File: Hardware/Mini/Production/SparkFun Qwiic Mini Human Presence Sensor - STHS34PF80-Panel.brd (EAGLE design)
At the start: 175 x 132.6 mm, 2112 parts, among them J1 Qwiic, J10 Qwiic, J100 Qwiic, J101 Qwiic, J103 Qwiic, J104 Qwiic, J106 Qwiic, J107 Qwiic, J109 Qwiic, J11 Qwiic, J110 Qwiic, J112 Qwiic, J113 Qwiic, J115 Qwiic, J116 Qwiic, J118 Qwiic, J119 Qwiic, J121 Qwiic, J122 Qwiic, J124 Qwiic, J125 Qwiic, J127 Qwiic, J128 Qwiic, J13 Qwiic, J130 Qwiic, J131 Qwiic, J133 Qwiic, J134 Qwiic, J136 Qwiic, J137 Qwiic, J139 Qwiic, J14 Qwiic, J140 Qwiic, J142 Qwiic, J143 Qwiic, J145 Qwiic, J146 Qwiic, J148 Qwiic, J149 Qwiic, J151 Qwiic, J152 Qwiic, J154 Qwiic, J155 Qwiic, J157 Qwiic, J158 Qwiic, J16 Qwiic, J160 Qwiic, J161 Qwiic, J17 Qwiic, J19 Qwiic, J2 Qwiic, J20 Qwiic, J22 Qwiic, J23 Qwiic, J25 Qwiic, J26 Qwiic, J28 Qwiic, J29 Qwiic, J31 Qwiic, J32 Qwiic, J34 Qwiic, J35 Qwiic, J37 Qwiic, J38 Qwiic, J4 Qwiic, J40 Qwiic, J41 Qwiic, J43 Qwiic, J44 Qwiic, J46 Qwiic, J47 Qwiic, J49 Qwiic, J5 Qwiic, J50 Qwiic, J52 Qwiic, J53 Qwiic, J55 Qwiic, J56 Qwiic, J58 Qwiic, J59 Qwiic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

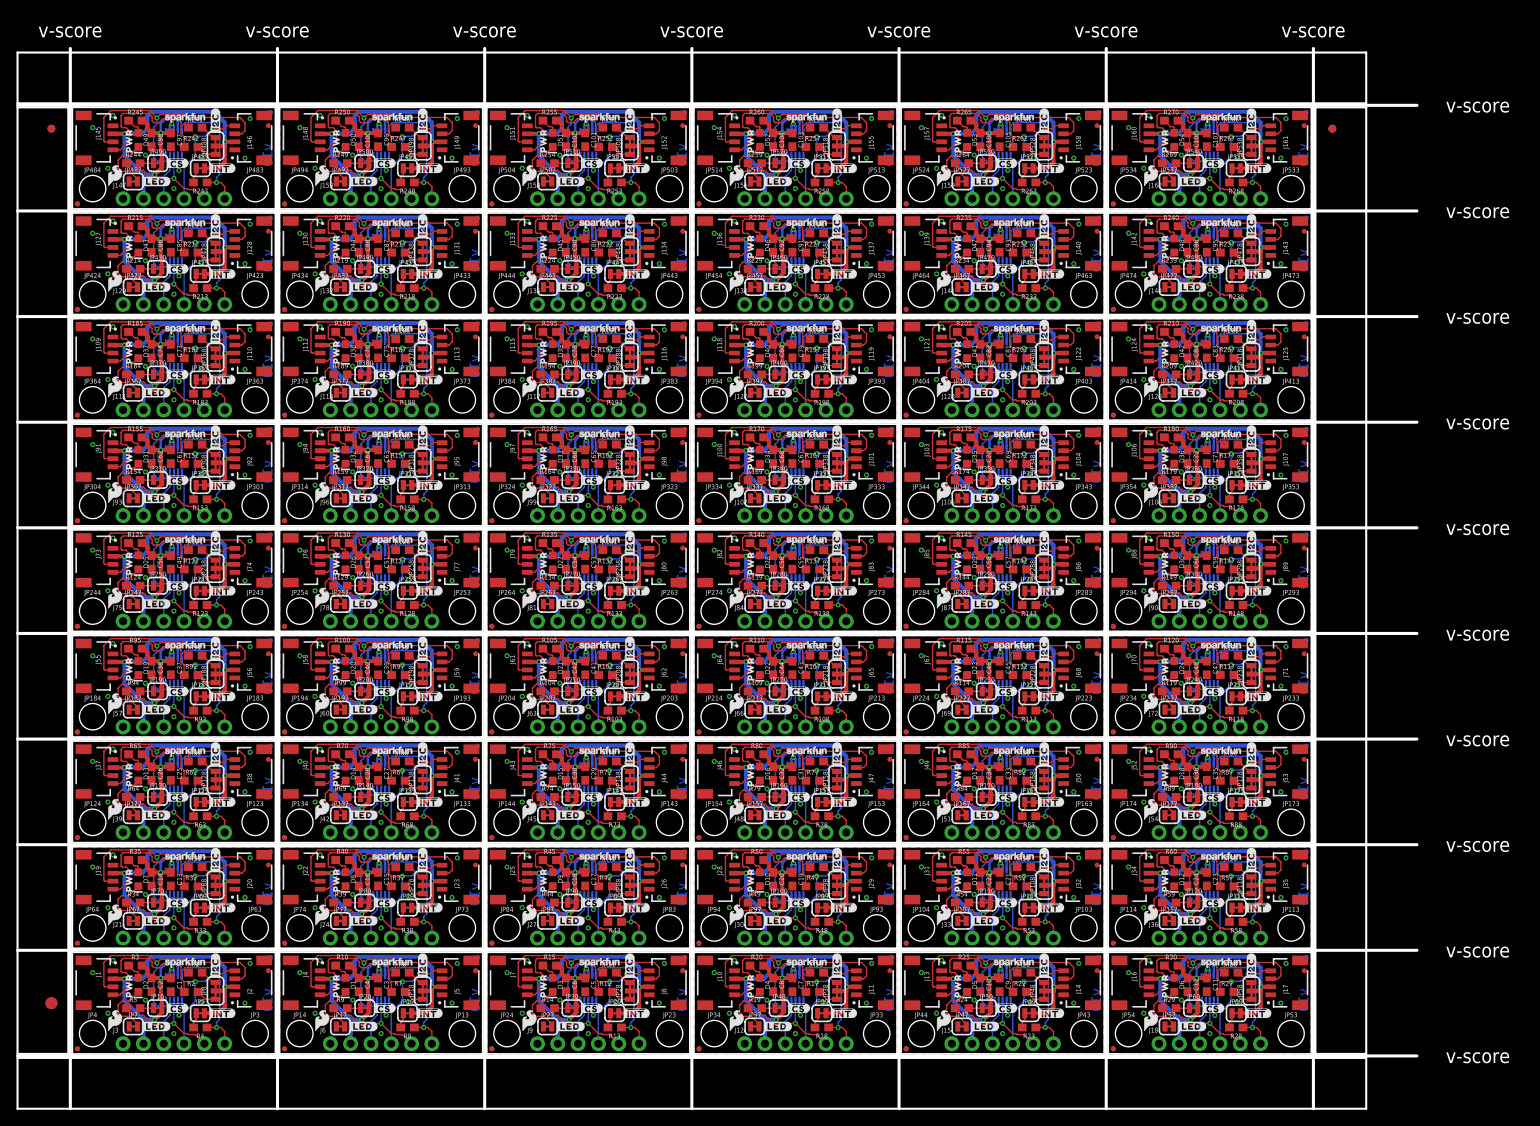
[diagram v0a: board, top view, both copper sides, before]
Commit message: Updated files for design review
Changed ST part to have 80% solder cream; changed panels to be 6x6 boards; changed vector font issues in schematic; added measures; added some more silk for easier part identification
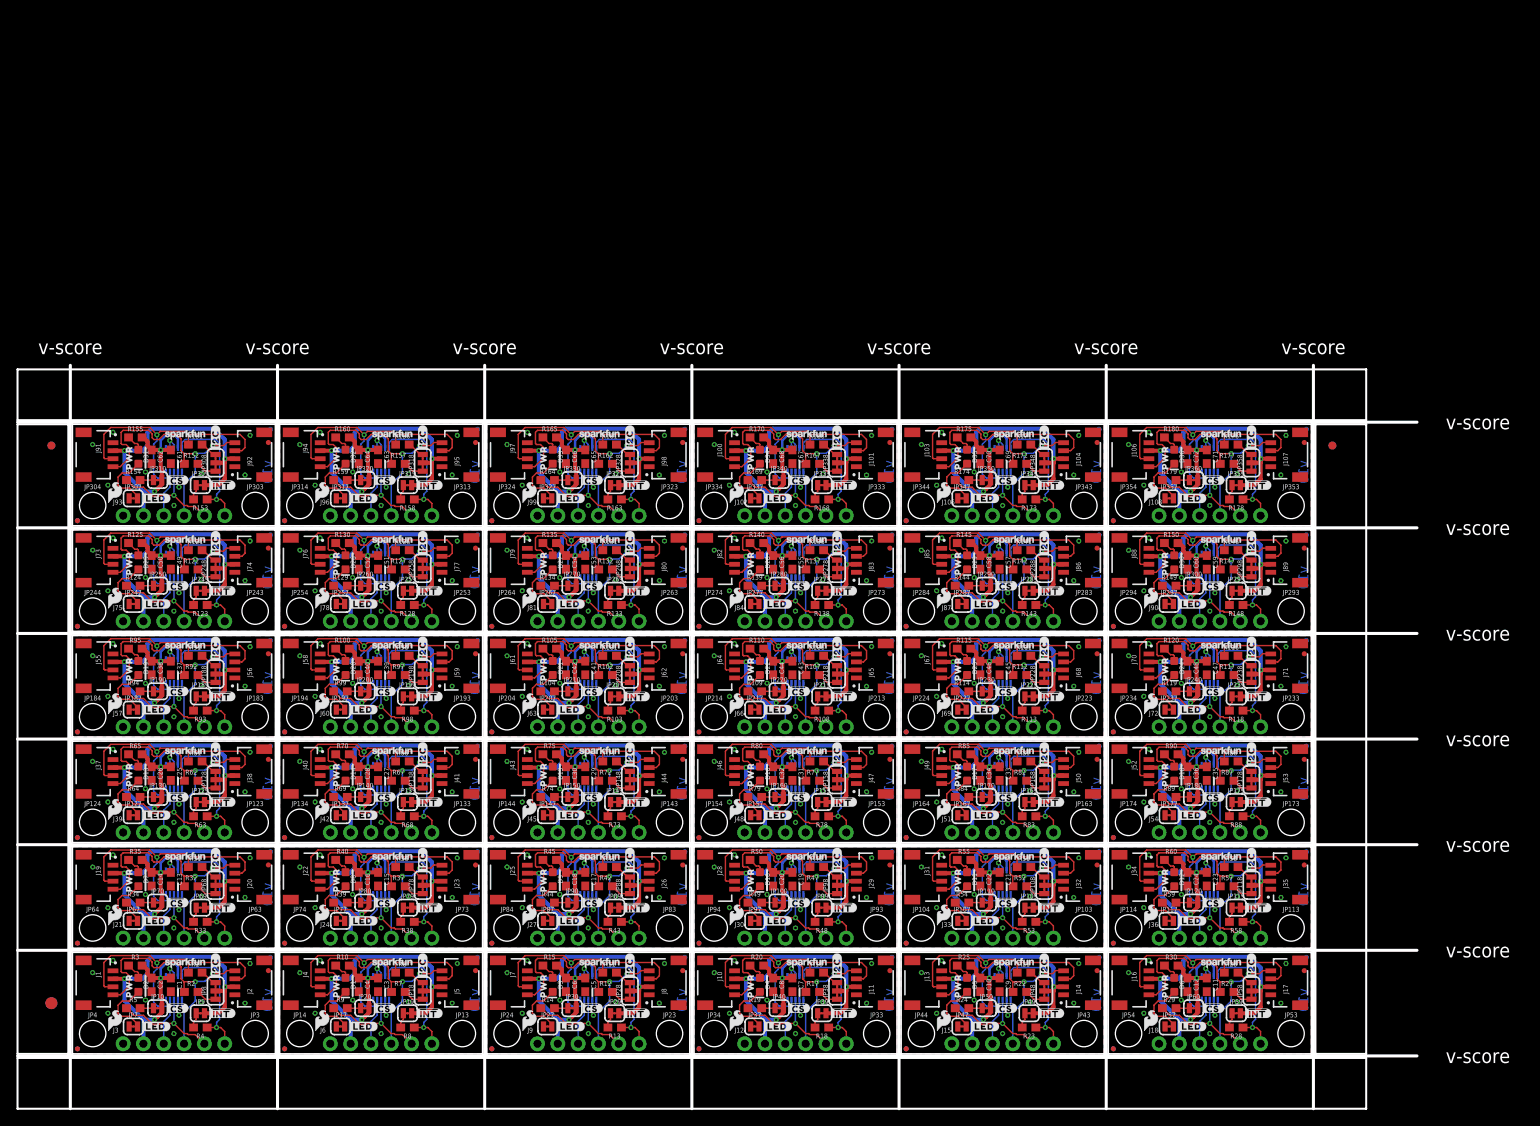
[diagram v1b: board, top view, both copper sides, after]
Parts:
- removed C100, C102, C104, C106, C108, C74, C76, C78, C80, C82, C84, C86, C88, C90, C92, C94, C96, C98: 0.1uF, SparkFun-Capacitors:0603
- removed C101, C103, C105, C107, C73, C75, C77, C79, C81, C83, C85, C87, C89, C91, C93, C95, C97, C99: 1.0uF, SparkFun-Capacitors:0603
- removed D37, D38, D39, D40, D41, D42, D43, D44, D45, D46, D47, D48, D49, D50, D51, D52, D53, D54: RED, SparkFun-LED:LED-0603
- removed J109, J110, J112, J113, J115, J116, J118, J119, J121, J122, J124, J125, J127, J128, J130, J131, J133, J134, J136, J137, J139, J140, J142, J143, J145, J146, J148, J149, J151, J152, J154, J155, J157, J158, J160, J161: Qwiic, SparkFun-Connectors:JST04_1MM_RA
- removed J111, J114, J117, J120, J123, J126, J129, J132, J135, J138, J141, J144, J147, J150, J153, J156, J159, J162: (no value), SparkFun-Connectors:1X06_NO_SILK
- removed JP361, JP362, JP365, JP366, JP371, JP372, JP375, JP376, JP381, JP382, JP385, JP386, JP391, JP392, JP395, JP396, JP401, JP402, JP405, JP406, JP411, JP412, JP415, JP416, JP421, JP422, JP425, JP426, JP431, JP432, JP435, JP436, JP441, JP442, JP445, JP446, JP451, JP452, JP455, JP456, JP461, JP462, JP465, JP466, JP471, JP472, JP475, JP476, JP481, JP482, JP485, JP486, JP491, JP492, JP495, JP496, JP501, JP502, JP505, JP506, JP511, JP512, JP515, JP516, JP521, JP522, JP525, JP526, JP531, JP532, JP535, JP536: FIDUCIALUFIDUCIAL, SparkFun-Aesthetics:FIDUCIAL-MICRO
- removed JP363, JP364, JP373, JP374, JP383, JP384, JP393, JP394, JP403, JP404, JP413, JP414, JP423, JP424, JP433, JP434, JP443, JP444, JP453, JP454, JP463, JP464, JP473, JP474, JP483, JP484, JP493, JP494, JP503, JP504, JP513, JP514, JP523, JP524, JP533, JP534: STAND-OFF, SparkFun-Hardware:STAND-OFF
- removed JP367, JP369, JP370, JP377, JP379, JP380, JP387, JP389, JP390, JP397, JP399, JP400, JP407, JP409, JP410, JP417, JP419, JP420, JP427, JP429, JP430, JP437, JP439, JP440, JP447, JP449, JP450, JP457, JP459, JP460, JP467, JP469, JP470, JP477, JP479, JP480, JP487, JP489, JP490, JP497, JP499, JP500, JP507, JP509, JP510, JP517, JP519, JP520, JP527, JP529, JP530, JP537, JP539, JP540: JUMPER-SMT_2_NC_TRACE_SILK, SparkFun-Jumpers:SMT-JUMPER_2_NC_TRACE_SILK
- removed JP368, JP378, JP388, JP398, JP408, JP418, JP428, JP438, JP448, JP458, JP468, JP478, JP488, JP498, JP508, JP518, JP528, JP538: JUMPER-SMT_3_2-NC_TRACE_SILK, SparkFun-Jumpers:SMT-JUMPER_3_2-NC_TRACE_SILK
- removed LOGO181, LOGO186, LOGO191, LOGO196, LOGO201, LOGO206, LOGO211, LOGO216, LOGO221, LOGO226, LOGO231, LOGO236, LOGO241, LOGO246, LOGO251, LOGO256, LOGO261, LOGO266: OSHW-LOGOS, SparkFun-Aesthetics:OSHW-LOGO-S
- removed LOGO182, LOGO187, LOGO192, LOGO197, LOGO202, LOGO207, LOGO212, LOGO217, LOGO222, LOGO227, LOGO232, LOGO237, LOGO242, LOGO247, LOGO252, LOGO257, LOGO262, LOGO267: QWIIC_LOGO_CONNECTOR, SparkFun-Aesthetics:QWIIC_5.5MM
- removed LOGO183, LOGO188, LOGO193, LOGO198, LOGO203, LOGO208, LOGO213, LOGO218, LOGO223, LOGO228, LOGO233, LOGO238, LOGO243, LOGO248, LOGO253, LOGO258, LOGO263, LOGO268: SFE_LOGO_NAME_FLAME7_MM, SparkFun-Aesthetics:SFE_LOGO_NAME_FLAME_7MM
- removed LOGO184, LOGO189, LOGO194, LOGO199, LOGO204, LOGO209, LOGO214, LOGO219, LOGO224, LOGO229, LOGO234, LOGO239, LOGO244, LOGO249, LOGO254, LOGO259, LOGO264, LOGO269: SFE_LOGO_FLAME.1_INCH, SparkFun-Aesthetics:SFE_LOGO_FLAME_.1
- removed LOGO185, LOGO190, LOGO195, LOGO200, LOGO205, LOGO210, LOGO215, LOGO220, LOGO225, LOGO230, LOGO235, LOGO240, LOGO245, LOGO250, LOGO255, LOGO260, LOGO265, LOGO270: SFE_LOGO_NAME5_MM, SparkFun-Aesthetics:SFE_LOGO_NAME_5MM
- removed R181, R182, R186, R187, R191, R192, R196, R197, R201, R202, R206, R207, R211, R212, R216, R217, R221, R222, R226, R227, R231, R232, R236, R237, R241, R242, R246, R247, R251, R252, R256, R257, R261, R262, R266, R267: 2.2k, SparkFun-Resistors:0603
- removed R183, R184, R188, R189, R193, R194, R198, R199, R203, R204, R208, R209, R213, R214, R218, R219, R223, R224, R228, R229, R233, R234, R238, R239, R243, R244, R248, R249, R253, R254, R258, R259, R263, R264, R268, R269: 10k, SparkFun-Resistors:0603
- removed R185, R190, R195, R200, R205, R210, R215, R220, R225, R230, R235, R240, R245, R250, R255, R260, R265, R270: 4.7k, SparkFun-Resistors:0603
- removed U$433, U$445, U$457, U$469, U$481, U$493, U$505, U$517, U$529, U$541, U$553, U$565, U$577, U$589, U$601, U$613, U$625, U$637: (no value), output:#SDA#5
- removed U$434, U$446, U$458, U$470, U$482, U$494, U$506, U$518, U$530, U$542, U$554, U$566, U$578, U$590, U$602, U$614, U$626, U$638: (no value), output:#SCL#6
- removed U$435, U$447, U$459, U$471, U$483, U$495, U$507, U$519, U$531, U$543, U$555, U$567, U$579, U$591, U$603, U$615, U$627, U$639: (no value), output:PWR9
- removed U$436, U$448, U$460, U$472, U$484, U$496, U$508, U$520, U$532, U$544, U$556, U$568, U$580, U$592, U$604, U$616, U$628, U$640: (no value), output:#I2C#0
- removed U$437, U$449, U$461, U$473, U$485, U$497, U$509, U$521, U$533, U$545, U$557, U$569, U$581, U$593, U$605, U$617, U$629, U$641: (no value), output:##CS#6
- removed U$438, U$450, U$462, U$474, U$486, U$498, U$510, U$522, U$534, U$546, U$558, U$570, U$582, U$594, U$606, U$618, U$630, U$642: (no value), output:#LED#8
- removed U$439, U$451, U$463, U$475, U$487, U$499, U$511, U$523, U$535, U$547, U$559, U$571, U$583, U$595, U$607, U$619, U$631, U$643: (no value), output:##INT#9
- removed U$440, U$452, U$464, U$476, U$488, U$500, U$512, U$524, U$536, U$548, U$560, U$572, U$584, U$596, U$608, U$620, U$632, U$644: (no value), output:STH34PF80_PRESENCE_SENSOR10
- removed U$441, U$453, U$465, U$477, U$489, U$501, U$513, U$525, U$537, U$549, U$561, U$573, U$585, U$597, U$609, U$621, U$633, U$645: (no value), output:#GND#35
- removed U$442, U$454, U$466, U$478, U$490, U$502, U$514, U$526, U$538, U$550, U$562, U$574, U$586, U$598, U$610, U$622, U$634, U$646: (no value), output:#3V3#36
- removed U$443, U$455, U$467, U$479, U$491, U$503, U$515, U$527, U$539, U$551, U$563, U$575, U$587, U$599, U$611, U$623, U$635, U$647: (no value), output:##CS#36
- removed U$444, U$456, U$468, U$480, U$492, U$504, U$516, U$528, U$540, U$552, U$564, U$576, U$588, U$600, U$612, U$624, U$636, U$648: (no value), output:#INT#37
- removed U37, U38, U39, U40, U41, U42, U43, U44, U45, U46, U47, U48, U49, U50, U51, U52, U53, U54: STHS34PF80, STHS34PF80:OLGA-10L
- moved E$1 39.6 mm to (-2.62, 76.1)
- moved E$2 39.6 mm to (-2.62, 76.1)
- moved E$3 39.6 mm to (157.6, 76.1)
- moved E$4 39.6 mm to (157.6, 76.1)
- moved U1 25.9 mm to (12.7, 8.26)
- moved U2 25.9 mm to (38.6, 8.26)
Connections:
- removed net !CS!36: J111.5, R184.1, U37.3
- removed net !CS!37: J114.5, R189.1, U38.3
- removed net !CS!38: J117.5, R194.1, U39.3
- removed net !CS!39: J120.5, R199.1, U40.3
- removed net !CS!40: J123.5, R204.1, U41.3
- removed net !CS!41: J126.5, R209.1, U42.3
- removed net !CS!42: J129.5, R214.1, U43.3
- removed net !CS!43: J132.5, R219.1, U44.3
- removed net !CS!44: J135.5, R224.1, U45.3
- removed net !CS!45: J138.5, R229.1, U46.3
- removed net !CS!46: J141.5, R234.1, U47.3
- removed net !CS!47: J144.5, R239.1, U48.3
- removed net !CS!48: J147.5, R244.1, U49.3
- removed net !CS!49: J150.5, R249.1, U50.3
- removed net !CS!50: J153.5, R254.1, U51.3
- removed net !CS!51: J156.5, R259.1, U52.3
- removed net !CS!52: J159.5, R264.1, U53.3
- removed net !CS!53: J162.5, R269.1, U54.3
- removed net 3.3V36: C73.1, C74.1, J109.2, J110.2, J111.2, JP368.2, JP369.2, JP370.2, R185.2, U37.6, U37.9
- removed net 3.3V37: C75.1, C76.1, J112.2, J113.2, J114.2, JP378.2, JP379.2, JP380.2, R190.2, U38.6, U38.9
- removed net 3.3V38: C77.1, C78.1, J115.2, J116.2, J117.2, JP388.2, JP389.2, JP390.2, R195.2, U39.6, U39.9
- removed net 3.3V39: C79.1, C80.1, J118.2, J119.2, J120.2, JP398.2, JP399.2, JP400.2, R200.2, U40.6, U40.9
- removed net 3.3V40: C81.1, C82.1, J121.2, J122.2, J123.2, JP408.2, JP409.2, JP410.2, R205.2, U41.6, U41.9
- removed net 3.3V41: C83.1, C84.1, J124.2, J125.2, J126.2, JP418.2, JP419.2, JP420.2, R210.2, U42.6, U42.9
- removed net 3.3V42: C85.1, C86.1, J127.2, J128.2, J129.2, JP428.2, JP429.2, JP430.2, R215.2, U43.6, U43.9
- removed net 3.3V43: C87.1, C88.1, J130.2, J131.2, J132.2, JP438.2, JP439.2, JP440.2, R220.2, U44.6, U44.9
- removed net 3.3V44: C89.1, C90.1, J133.2, J134.2, J135.2, JP448.2, JP449.2, JP450.2, R225.2, U45.6, U45.9
- removed net 3.3V45: C91.1, C92.1, J136.2, J137.2, J138.2, JP458.2, JP459.2, JP460.2, R230.2, U46.6, U46.9
- removed net 3.3V46: C93.1, C94.1, J139.2, J140.2, J141.2, JP468.2, JP469.2, JP470.2, R235.2, U47.6, U47.9
- removed net 3.3V47: C95.1, C96.1, J142.2, J143.2, J144.2, JP478.2, JP479.2, JP480.2, R240.2, U48.6, U48.9
- removed net 3.3V48: C97.1, C98.1, J145.2, J146.2, J147.2, JP488.2, JP489.2, JP490.2, R245.2, U49.6, U49.9
- removed net 3.3V49: C100.1, C99.1, J148.2, J149.2, J150.2, JP498.2, JP499.2, JP500.2, R250.2, U50.6, U50.9
- removed net 3.3V50: C101.1, C102.1, J151.2, J152.2, J153.2, JP508.2, JP509.2, JP510.2, R255.2, U51.6, U51.9
- removed net 3.3V51: C103.1, C104.1, J154.2, J155.2, J156.2, JP518.2, JP519.2, JP520.2, R260.2, U52.6, U52.9
- removed net 3.3V52: C105.1, C106.1, J157.2, J158.2, J159.2, JP528.2, JP529.2, JP530.2, R265.2, U53.6, U53.9
- removed net 3.3V53: C107.1, C108.1, J160.2, J161.2, J162.2, JP538.2, JP539.2, JP540.2, R270.2, U54.6, U54.9
- removed net GND36: C73.2, C74.2, J109.1, J110.1, J111.1, JP367.1, U37.2, U37.7, U37.8
- removed net GND37: C75.2, C76.2, J112.1, J113.1, J114.1, JP377.1, U38.2, U38.7, U38.8
- removed net GND38: C77.2, C78.2, J115.1, J116.1, J117.1, JP387.1, U39.2, U39.7, U39.8
- removed net GND39: C79.2, C80.2, J118.1, J119.1, J120.1, JP397.1, U40.2, U40.7, U40.8
- removed net GND40: C81.2, C82.2, J121.1, J122.1, J123.1, JP407.1, U41.2, U41.7, U41.8
- removed net GND41: C83.2, C84.2, J124.1, J125.1, J126.1, JP417.1, U42.2, U42.7, U42.8
- removed net GND42: C85.2, C86.2, J127.1, J128.1, J129.1, JP427.1, U43.2, U43.7, U43.8
- removed net GND43: C87.2, C88.2, J130.1, J131.1, J132.1, JP437.1, U44.2, U44.7, U44.8
- removed net GND44: C89.2, C90.2, J133.1, J134.1, J135.1, JP447.1, U45.2, U45.7, U45.8
- removed net GND45: C91.2, C92.2, J136.1, J137.1, J138.1, JP457.1, U46.2, U46.7, U46.8
- removed net GND46: C93.2, C94.2, J139.1, J140.1, J141.1, JP467.1, U47.2, U47.7, U47.8
- removed net GND47: C95.2, C96.2, J142.1, J143.1, J144.1, JP477.1, U48.2, U48.7, U48.8
- removed net GND48: C97.2, C98.2, J145.1, J146.1, J147.1, JP487.1, U49.2, U49.7, U49.8
- removed net GND49: C100.2, C99.2, J148.1, J149.1, J150.1, JP497.1, U50.2, U50.7, U50.8
- removed net GND50: C101.2, C102.2, J151.1, J152.1, J153.1, JP507.1, U51.2, U51.7, U51.8
- removed net GND51: C103.2, C104.2, J154.1, J155.1, J156.1, JP517.1, U52.2, U52.7, U52.8
- removed net GND52: C105.2, C106.2, J157.1, J158.1, J159.1, JP527.1, U53.2, U53.7, U53.8
- removed net GND53: C107.2, C108.2, J160.1, J161.1, J162.1, JP537.1, U54.2, U54.7, U54.8
- removed net INT36: J111.6, R183.1, U37.10
- removed net INT37: J114.6, R188.1, U38.10
- removed net INT38: J117.6, R193.1, U39.10
- removed net INT39: J120.6, R198.1, U40.10
- removed net INT40: J123.6, R203.1, U41.10
- removed net INT41: J126.6, R208.1, U42.10
- removed net INT42: J129.6, R213.1, U43.10
- removed net INT43: J132.6, R218.1, U44.10
- removed net INT44: J135.6, R223.1, U45.10
- removed net INT45: J138.6, R228.1, U46.10
- removed net INT46: J141.6, R233.1, U47.10
- removed net INT47: J144.6, R238.1, U48.10
- removed net INT48: J147.6, R243.1, U49.10
- removed net INT49: J150.6, R248.1, U50.10
- removed net INT50: J153.6, R253.1, U51.10
- removed net INT51: J156.6, R258.1, U52.10
- removed net INT52: J159.6, R263.1, U53.10
- removed net INT53: J162.6, R268.1, U54.10
- removed net N$217: JP368.3, R181.2
- removed net N$218: JP368.1, R182.2
- removed net N$219: D37.A, R185.1
- removed net N$220: JP369.1, R183.2
- removed net N$221: D37.C, JP367.2
- removed net N$222: JP370.1, R184.2
- removed net N$223: JP378.3, R186.2
- removed net N$224: JP378.1, R187.2
- removed net N$225: D38.A, R190.1
- removed net N$226: JP379.1, R188.2
- removed net N$227: D38.C, JP377.2
- removed net N$228: JP380.1, R189.2
- removed net N$229: JP388.3, R191.2
- removed net N$230: JP388.1, R192.2
- removed net N$231: D39.A, R195.1
- removed net N$232: JP389.1, R193.2
- removed net N$233: D39.C, JP387.2
- removed net N$234: JP390.1, R194.2
- removed net N$235: JP398.3, R196.2
- removed net N$236: JP398.1, R197.2
- removed net N$237: D40.A, R200.1
- removed net N$238: JP399.1, R198.2
- removed net N$239: D40.C, JP397.2
- removed net N$240: JP400.1, R199.2
- removed net N$241: JP408.3, R201.2
- removed net N$242: JP408.1, R202.2
- removed net N$243: D41.A, R205.1
- removed net N$244: JP409.1, R203.2
- removed net N$245: D41.C, JP407.2
- removed net N$246: JP410.1, R204.2
- removed net N$247: JP418.3, R206.2
- removed net N$248: JP418.1, R207.2
- removed net N$249: D42.A, R210.1
- removed net N$250: JP419.1, R208.2
- removed net N$251: D42.C, JP417.2
- removed net N$252: JP420.1, R209.2
- removed net N$253: JP428.3, R211.2
- removed net N$254: JP428.1, R212.2
- removed net N$255: D43.A, R215.1
- removed net N$256: JP429.1, R213.2
- removed net N$257: D43.C, JP427.2
- removed net N$258: JP430.1, R214.2
- removed net N$259: JP438.3, R216.2
- removed net N$260: JP438.1, R217.2
- removed net N$261: D44.A, R220.1
- removed net N$262: JP439.1, R218.2
- removed net N$263: D44.C, JP437.2
- removed net N$264: JP440.1, R219.2
- removed net N$265: JP448.3, R221.2
- removed net N$266: JP448.1, R222.2
- removed net N$267: D45.A, R225.1
- removed net N$268: JP449.1, R223.2
- removed net N$269: D45.C, JP447.2
- removed net N$270: JP450.1, R224.2
- removed net N$271: JP458.3, R226.2
- removed net N$272: JP458.1, R227.2
- removed net N$273: D46.A, R230.1
- removed net N$274: JP459.1, R228.2
- removed net N$275: D46.C, JP457.2
- removed net N$276: JP460.1, R229.2
- removed net N$277: JP468.3, R231.2
- removed net N$278: JP468.1, R232.2
- removed net N$279: D47.A, R235.1
- removed net N$280: JP469.1, R233.2
- removed net N$281: D47.C, JP467.2
- removed net N$282: JP470.1, R234.2
- removed net N$283: JP478.3, R236.2
- removed net N$284: JP478.1, R237.2
- removed net N$285: D48.A, R240.1
- removed net N$286: JP479.1, R238.2
- removed net N$287: D48.C, JP477.2
- removed net N$288: JP480.1, R239.2
- removed net N$289: JP488.3, R241.2
- removed net N$290: JP488.1, R242.2
- removed net N$291: D49.A, R245.1
- removed net N$292: JP489.1, R243.2
- removed net N$293: D49.C, JP487.2
- removed net N$294: JP490.1, R244.2
- removed net N$295: JP498.3, R246.2
- removed net N$296: JP498.1, R247.2
- removed net N$297: D50.A, R250.1
- removed net N$298: JP499.1, R248.2
- removed net N$299: D50.C, JP497.2
- removed net N$300: JP500.1, R249.2
- removed net N$301: JP508.3, R251.2
- removed net N$302: JP508.1, R252.2
- removed net N$303: D51.A, R255.1
- removed net N$304: JP509.1, R253.2
- removed net N$305: D51.C, JP507.2
- removed net N$306: JP510.1, R254.2
- removed net N$307: JP518.3, R256.2
- removed net N$308: JP518.1, R257.2
- removed net N$309: D52.A, R260.1
- removed net N$310: JP519.1, R258.2
- removed net N$311: D52.C, JP517.2
- removed net N$312: JP520.1, R259.2
- removed net N$313: JP528.3, R261.2
- removed net N$314: JP528.1, R262.2
- removed net N$315: D53.A, R265.1
- removed net N$316: JP529.1, R263.2
- removed net N$317: D53.C, JP527.2
- removed net N$318: JP530.1, R264.2
- removed net N$319: JP538.3, R266.2
- removed net N$320: JP538.1, R267.2
- removed net N$321: D54.A, R270.1
- removed net N$322: JP539.1, R268.2
- removed net N$323: D54.C, JP537.2
- removed net N$324: JP540.1, R269.2
- removed net SCL36: J109.4, J110.4, J111.4, R182.1, U37.1
- removed net SCL37: J112.4, J113.4, J114.4, R187.1, U38.1
- removed net SCL38: J115.4, J116.4, J117.4, R192.1, U39.1
- removed net SCL39: J118.4, J119.4, J120.4, R197.1, U40.1
- removed net SCL40: J121.4, J122.4, J123.4, R202.1, U41.1
- removed net SCL41: J124.4, J125.4, J126.4, R207.1, U42.1
- removed net SCL42: J127.4, J128.4, J129.4, R212.1, U43.1
- removed net SCL43: J130.4, J131.4, J132.4, R217.1, U44.1
- removed net SCL44: J133.4, J134.4, J135.4, R222.1, U45.1
- removed net SCL45: J136.4, J137.4, J138.4, R227.1, U46.1
- removed net SCL46: J139.4, J140.4, J141.4, R232.1, U47.1
- removed net SCL47: J142.4, J143.4, J144.4, R237.1, U48.1
- removed net SCL48: J145.4, J146.4, J147.4, R242.1, U49.1
- removed net SCL49: J148.4, J149.4, J150.4, R247.1, U50.1
- removed net SCL50: J151.4, J152.4, J153.4, R252.1, U51.1
- removed net SCL51: J154.4, J155.4, J156.4, R257.1, U52.1
- removed net SCL52: J157.4, J158.4, J159.4, R262.1, U53.1
- removed net SCL53: J160.4, J161.4, J162.4, R267.1, U54.1
- removed net SDA36: J109.3, J110.3, J111.3, R181.1, U37.4
- removed net SDA37: J112.3, J113.3, J114.3, R186.1, U38.4
- removed net SDA38: J115.3, J116.3, J117.3, R191.1, U39.4
- removed net SDA39: J118.3, J119.3, J120.3, R196.1, U40.4
- removed net SDA40: J121.3, J122.3, J123.3, R201.1, U41.4
- removed net SDA41: J124.3, J125.3, J126.3, R206.1, U42.4
- removed net SDA42: J127.3, J128.3, J129.3, R211.1, U43.4
- removed net SDA43: J130.3, J131.3, J132.3, R216.1, U44.4
- removed net SDA44: J133.3, J134.3, J135.3, R221.1, U45.4
- removed net SDA45: J136.3, J137.3, J138.3, R226.1, U46.4
- removed net SDA46: J139.3, J140.3, J141.3, R231.1, U47.4
- removed net SDA47: J142.3, J143.3, J144.3, R236.1, U48.4
- removed net SDA48: J145.3, J146.3, J147.3, R241.1, U49.4
- removed net SDA49: J148.3, J149.3, J150.3, R246.1, U50.4
- removed net SDA50: J151.3, J152.3, J153.3, R251.1, U51.4
- removed net SDA51: J154.3, J155.3, J156.3, R256.1, U52.4
- removed net SDA52: J157.3, J158.3, J159.3, R261.1, U53.4
- removed net SDA53: J160.3, J161.3, J162.3, R266.1, U54.4
- net !CS!: now also U1.3; no longer U2.3
- net !CS!1: now also U2.3; no longer U1.3
- net 3.3V: now also U1.6, U1.9; no longer U2.6, U2.9
- net 3.3V1: now also U2.6, U2.9; no longer U1.6, U1.9
- net GND: now also U1.2, U1.7, U1.8; no longer U2.2, U2.7, U2.8
- net GND1: now also U2.2, U2.7, U2.8; no longer U1.2, U1.7, U1.8
- net INT: now also U1.10; no longer U2.10
- net INT1: now also U2.10; no longer U1.10
- net SCL: now also U1.1; no longer U2.1
- net SCL1: now also U2.1; no longer U1.1
- net SDA: now also U1.4; no longer U2.4
- net SDA1: now also U2.4; no longer U1.4
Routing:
- net 3.3V47: track 54.0 -> 0.00 mm, vias 4 -> 0
- net 3.3V45: track 54.0 -> 0.00 mm, vias 4 -> 0
- net 3.3V41: track 54.0 -> 0.00 mm, vias 4 -> 0
- net 3.3V39: track 54.0 -> 0.00 mm, vias 4 -> 0
- net 3.3V51: track 54.0 -> 0.00 mm, vias 4 -> 0
- net 3.3V53: track 54.0 -> 0.00 mm, vias 4 -> 0
- net 3.3V43: track 54.0 -> 0.00 mm, vias 4 -> 0
- net 3.3V42: track 54.0 -> 0.00 mm, vias 4 -> 0
- net 3.3V37: track 54.0 -> 0.00 mm, vias 4 -> 0
- net 3.3V36: track 54.0 -> 0.00 mm, vias 4 -> 0
- net 3.3V46: track 54.0 -> 0.00 mm, vias 4 -> 0
- net 3.3V44: track 54.0 -> 0.00 mm, vias 4 -> 0
- net 3.3V40: track 54.0 -> 0.00 mm, vias 4 -> 0
- net 3.3V38: track 54.0 -> 0.00 mm, vias 4 -> 0
- net 3.3V52: track 54.0 -> 0.00 mm, vias 4 -> 0
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- removed copper zone on layer 1, net GND36
- removed copper zone on layer 16, net GND36
- removed copper zone on layer 1, net GND37
- removed copper zone on layer 16, net GND37
- removed copper zone on layer 1, net GND38
- removed copper zone on layer 16, net GND38
- removed copper zone on layer 1, net GND39
- removed copper zone on layer 16, net GND39
- removed copper zone on layer 1, net GND40
- removed copper zone on layer 16, net GND40
- removed copper zone on layer 1, net GND41
- removed copper zone on layer 16, net GND41
- removed copper zone on layer 1, net GND42
- removed copper zone on layer 16, net GND42
- removed copper zone on layer 1, net GND43
- removed copper zone on layer 16, net GND43
- removed copper zone on layer 1, net GND44
- removed copper zone on layer 16, net GND44
- removed copper zone on layer 1, net GND45
- removed copper zone on layer 16, net GND45
- removed copper zone on layer 1, net GND46
- removed copper zone on layer 16, net GND46
- removed copper zone on layer 1, net GND47
- removed copper zone on layer 16, net GND47
- removed copper zone on layer 1, net GND48
- removed copper zone on layer 16, net GND48
- removed copper zone on layer 1, net GND49
- removed copper zone on layer 16, net GND49
- removed copper zone on layer 1, net GND50
- removed copper zone on layer 16, net GND50
- removed copper zone on layer 1, net GND51
- removed copper zone on layer 16, net GND51
- removed copper zone on layer 1, net GND52
- removed copper zone on layer 16, net GND52
- removed copper zone on layer 1, net GND53
- removed copper zone on layer 16, net GND53
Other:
- board size 175 x 132.6 mm -> 175 x 93 mm
